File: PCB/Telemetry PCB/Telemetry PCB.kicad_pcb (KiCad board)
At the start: 2 copper layers, 47 parts, among them IC1 E22-900M22S, J1 Conn_01x04_Pin, J2 Serial Debug Header 1x4, J3 GPS, J4 Batt, J5 USB_C_Receptacle_USB2.0_16P, SW1 SW_MEC_5E, SW2 SW_MEC_5E, U1 STM32F411CEUx, U2 MCP1700x-250xxTT, U3 AP62200WU, Y1 25MHZ 20pF, Y2 32.768k 12.5pF

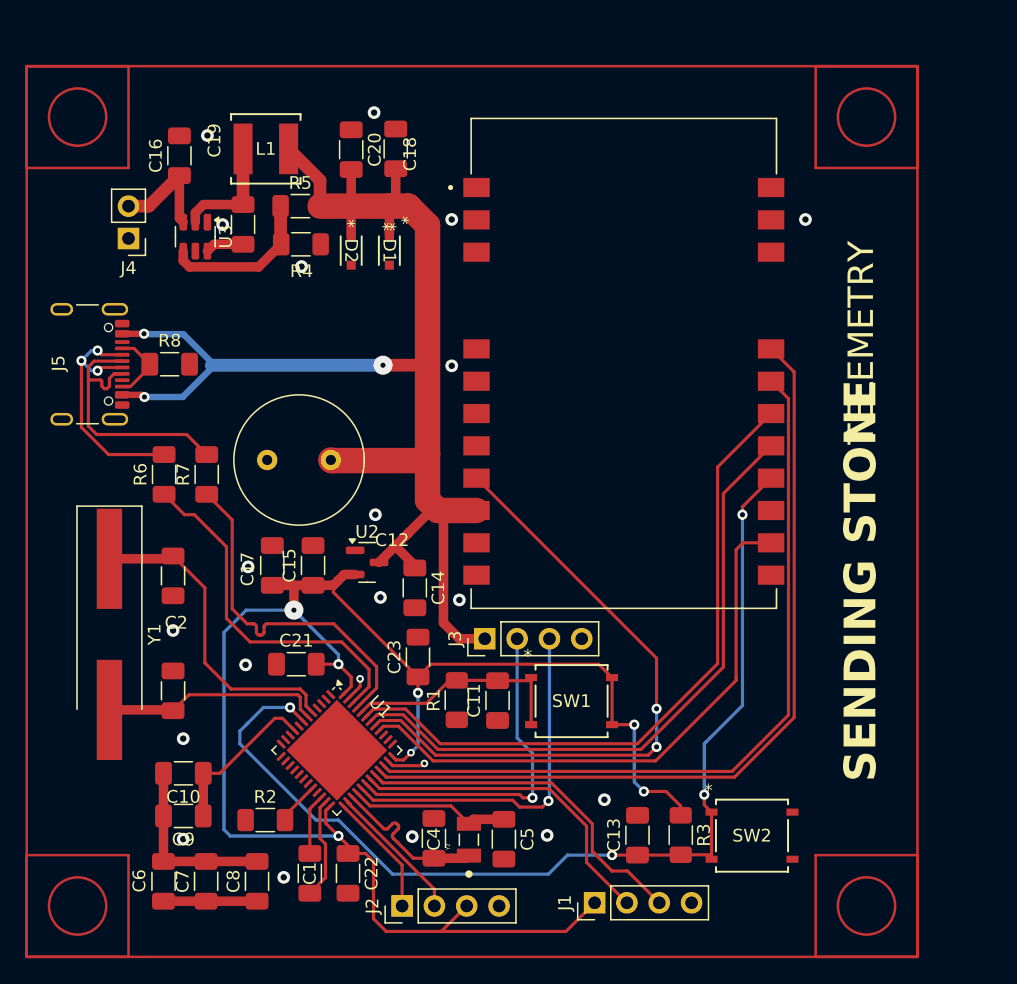
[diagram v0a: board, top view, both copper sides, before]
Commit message: Updated silkscreen and fixed front plane islands
Updated silkscreen and fixed front plane islands
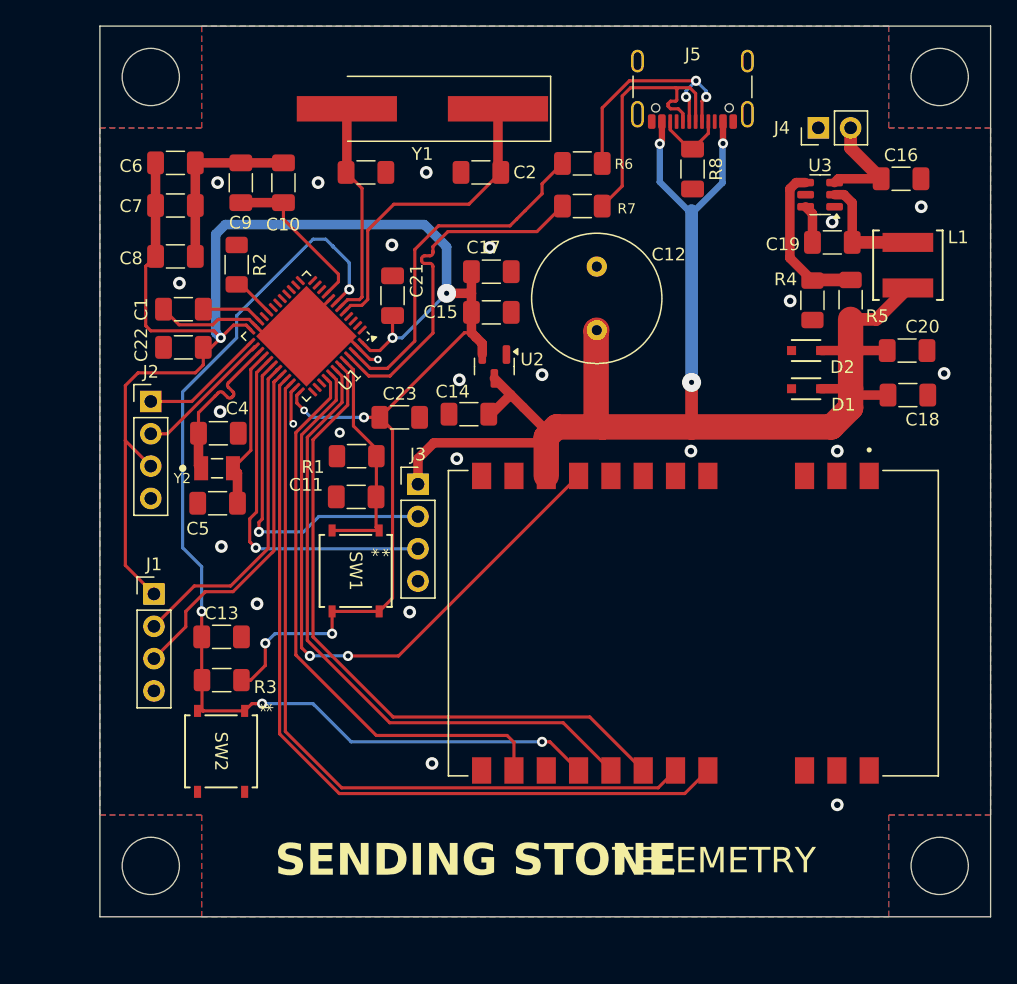
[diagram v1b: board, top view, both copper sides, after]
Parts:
- C21, C22, C23: value C -> 100nF
- moved C16 56.7 mm to (159.2, 102.1), turned to 0 degrees
- moved C6 56.5 mm to (102.2, 100.8), turned to 0 degrees
- moved J4 54.9 mm to (152.7, 98.1), turned to 90 degrees
- moved J5 53.6 mm to (142.8, 93.9), turned to 180 degrees
- moved C7 53.2 mm to (102.2, 104.2), turned to 0 degrees
- moved L1 51.3 mm to (159.8, 108.9), turned to -90 degrees
- moved C9 50.0 mm to (107.3, 102.4), turned to 90 degrees
- moved C8 49.5 mm to (102.2, 108.2), turned to 0 degrees
- moved U3 49.2 mm to (152.8, 103.3), turned to 180 degrees
- moved Y1 48.1 mm to (121.6, 96.6), turned to 180 degrees
- moved C10 47.1 mm to (110.7, 102.4), turned to 90 degrees
- moved C20 46.5 mm to (159.7, 115.6), turned to 180 degrees
- moved C19 46.3 mm to (153.8, 107.1), turned to 0 degrees
- moved C1 45.4 mm to (102.8, 112.3), turned to 0 degrees
- moved C18 44.7 mm to (159.8, 119.1), turned to 180 degrees
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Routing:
- net GND: track 27.5 -> 39.9 mm, vias 21 -> 24
- net +3.3V: track 140.3 -> 152.6 mm
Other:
- board outline added: 70 x 70 mm

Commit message: reannotated based on board geometry
reannotated based on board geometry
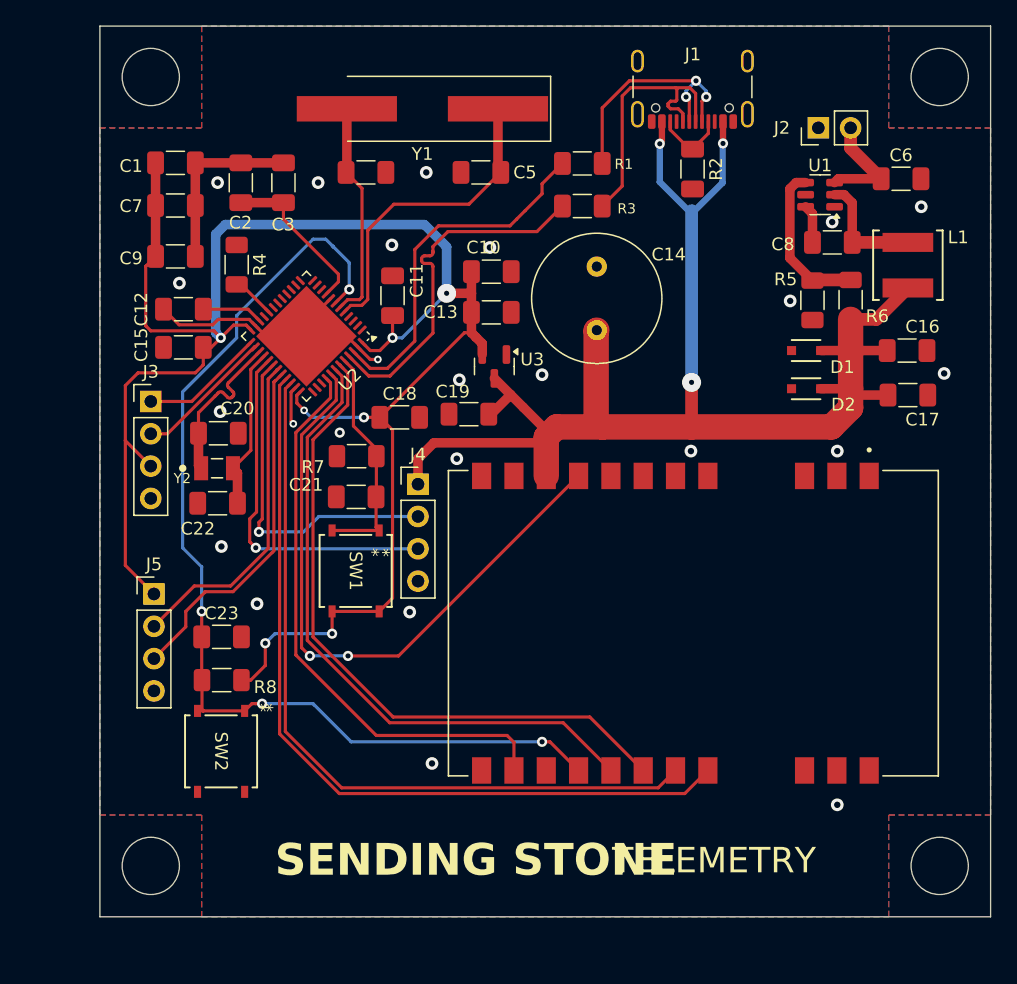
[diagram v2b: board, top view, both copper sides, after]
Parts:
- renumbered C6 to C1, C17 to C10, C21 to C11, C1 to C12, C15 to C13, C12 to C14, C22 to C15, C20 to C16, C18 to C17, C23 to C18, C14 to C19, C9 to C2, C4 to C20, C11 to C21, C5 to C22, C13 to C23, C10 to C3, C3 to C4, C2 to C5, C16 to C6, C19 to C8, C8 to C9, D2 to D1, D1 to D2, J5 to J1, J4 to J2, J2 to J3, J3 to J4, J1 to J5, R6 to R1, R8 to R2, R7 to R3, R2 to R4, R4 to R5, R5 to R6, R1 to R7, R3 to R8, U3 to U1, U1 to U2, U2 to U3

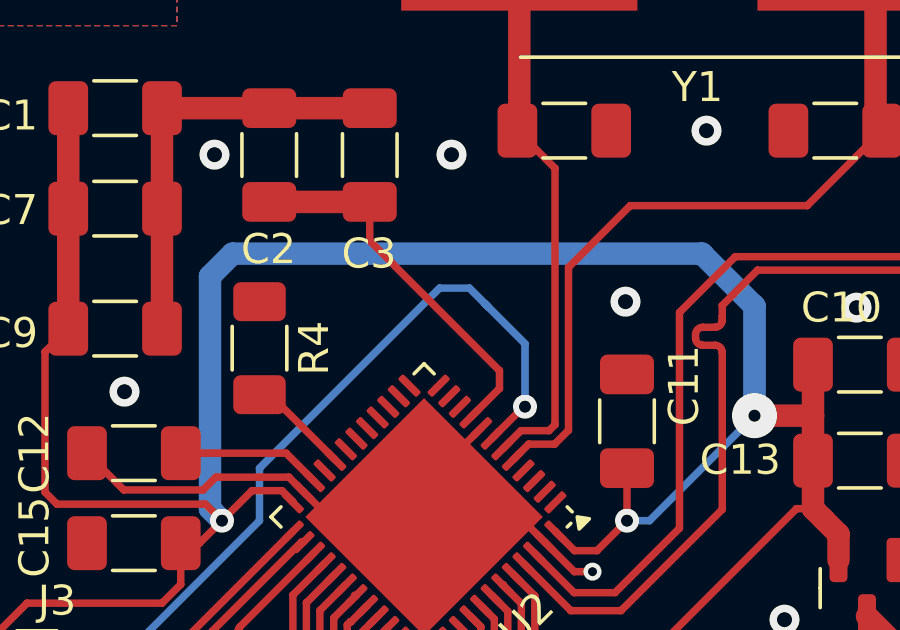
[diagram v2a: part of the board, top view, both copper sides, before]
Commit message: Added missing Gnd trace on Stm32
Added missing Gnd trace on Stm32
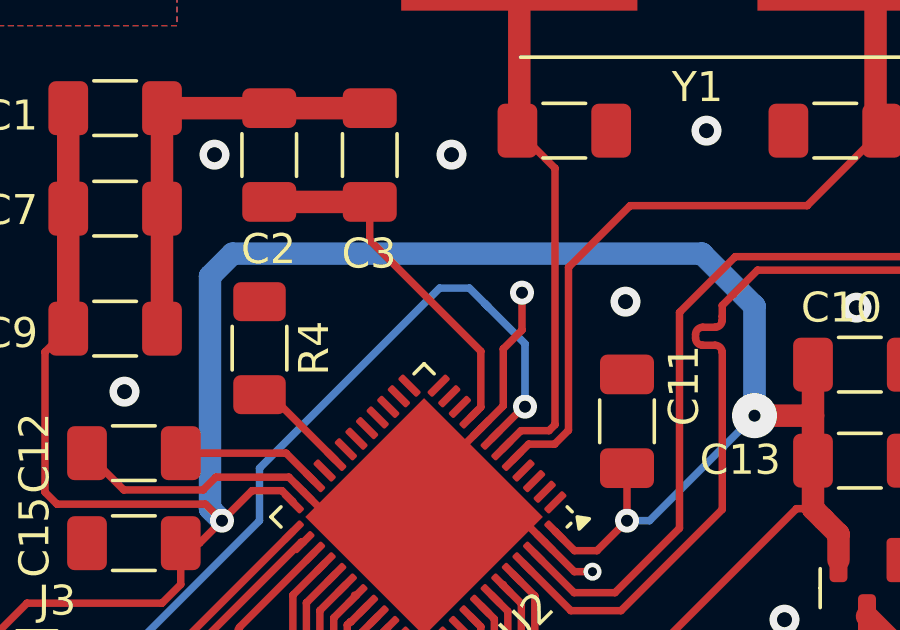
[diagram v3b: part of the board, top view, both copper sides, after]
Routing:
- net GND: track 39.9 -> 45.0 mm, vias 24 -> 25
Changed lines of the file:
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@@
+	)
+	(segment
+		(start 115.75 108.25)
+		(end 115.75 107)
+		(width 0.25)
+		(layer "F.Cu")
+		(net 1)
 	)
 	(segment
@@
 	)
 	(segment
+		(start 115.125 108.875)
+		(end 115.75 108.25)
+		(width 0.25)
+		(layer "F.Cu")
+		(net 1)
+	)
+	(segment
 		(start 103.749999 100.85)
 		(end 107.324999 100.849999)
@@
 	)
 	(segment
+		(start 115.125 110.775252)
+		(end 115.125 108.875)
+		(width 0.25)
+		(layer "F.Cu")
+		(net 1)
+	)
+	(segment
 		(start 111.275 118.867894)
 		(end 111.646447 118.496447)
@@
 		(start 105.55 113.15)
 		(end 105.125 113.575)
+		(width 0.25)
+		(layer "F.Cu")
+		(net 1)
+	)
+	(segment
+		(start 114.386485 111.513767)
+		(end 115.125 110.775252)
 		(width 0.25)
 		(layer "F.Cu")
@@
 	(via
 		(at 115.1 122.05)
+		(size 0.8)
+		(drill 0.4)
+		(layers "F.Cu" "B.Cu")
+		(free yes)
+		(net 1)
+	)
+	(via
+		(at 115.75 107)
 		(size 0.8)
 		(drill 0.4)
@@
 	)
 	(segment
-		(start 115 110.193146)
-		(end 115 109.6)
+		(start 110.675 105.25)
+		(end 110.675 103.975)
 		(width 0.25)
 		(layer "F.Cu")
@@
 	)
 	(segment
+		(start 114.377463 108.952463)
+		(end 110.675 105.25)
+		(width 0.25)
+		(layer "F.Cu")
+		(net 8)
+	)
+	(segment
+		(start 114.377463 110.815683)
+		(end 114.377463 108.952463)
+		(width 0.25)
+		(layer "F.Cu")
+		(net 8)
+	)
+	(segment
 		(start 110.675 105.274999)
-		(end 110.675 103.975)
-		(width 0.25)
-		(layer "F.Cu")
-		(net 8)
-	)
-	(segment
-		(start 115 109.6)
-		(end 110.675 105.274999)
+		(end 110.675 105.25)
 		(width 0.25)
 		(layer "F.Cu")
@@
 	(segment
 		(start 114.032932 111.160214)
-		(end 115 110.193146)
-		(width 0.25)
-		(layer "F.Cu")
+		(end 114.377463 110.815683)
+		(width 0.25)
+		(layer "F.Cu")

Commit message: Tweaked usb and data traces
Tweaked usb board should be able to be powered by usb without catching fire

I also moved some data traces away from each other and filled between them to lower their parasitic capacitance
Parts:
- added R9: 5.1k, Capacitor_SMD:C_1206_3216Metric_Pad1.33x1.80mm_HandSolder, F.Cu at (141.5, 102.3)
- moved R2 1.53 mm to (144.0, 102.3)
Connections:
- J1 pad A5: Net-(J5-CC1) -> Net-(J1-CC1)
- J1 pad B5: Net-(J5-CC1) -> Net-(J1-CC2)
- R2 pad 1: Net-(J5-CC1) -> Net-(J1-CC1)
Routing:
- net Net-(J5-CC1): track 5.71 -> 0.00 mm
- net +5V: track 113.9 -> 118.3 mm, vias 3 -> 7
- net Net-(J1-CC2): track 0.00 -> 3.32 mm
- net Net-(J1-CC1): track 0.00 -> 3.17 mm
- net NSS: track 64.5 -> 67.4 mm
- net GND: track 45.0 -> 45.8 mm, vias 25 -> 28
